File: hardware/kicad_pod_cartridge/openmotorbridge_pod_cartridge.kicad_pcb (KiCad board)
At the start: 2 copper layers, 35 x 25 mm, 28 parts, among them J1 POD_BASE_DOCKING_SOCKET_6P, J2 INTERCOM_HEADSET_6P, Q1 AO3400A, Q2 AO3400A, Q3 AO3400A, Q4 AO3400A, U1 CH32V003F4P6

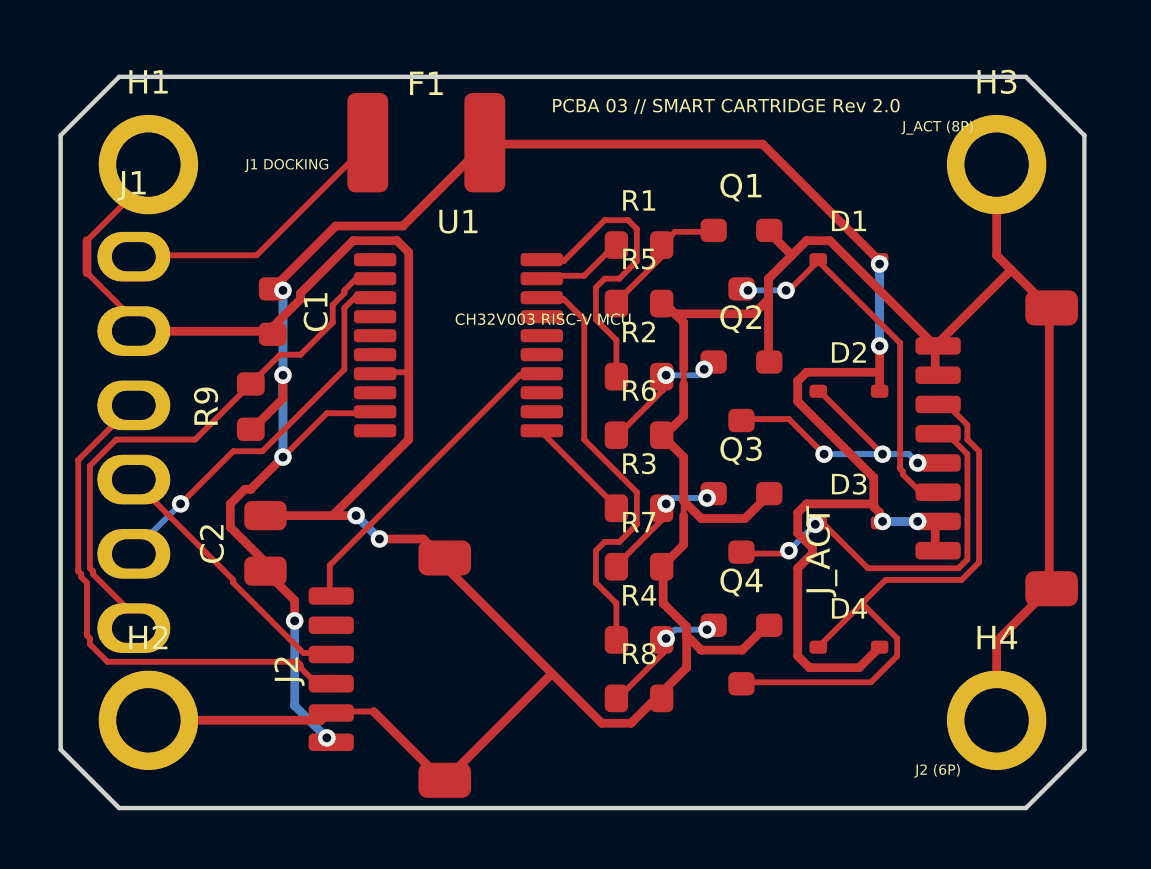
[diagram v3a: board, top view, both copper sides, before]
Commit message: hardware(pcb): synchronize 5-PCBA lineup with v9.6 All-UWB architecture
- PCBA 01 (Central Box): replace obsolete 26-pin IDC header with 12-pin Deutsch DTM-12 header (exact 12-pin net mapping), add 38.4MHz UWB crystal on B.Cu, update silkscreen and schematic
- PCBA 05 (Front Node): place Qorvo DW3110 + U.FL + crystal on B.Cu; place u-blox SAM-M10Q GNSS + Knowles MEMS mic on F.Cu
- PCBA 03 (Pod Cartridge): replace obsolete 6-pin dock socket with PAD1/PAD2 DC spring contact pads; place DW3110 + U.FL on B.Cu
- PCBA 08 (Radar Sub-MCU): update J1 to 2-pin 12V automotive power connector; place DW3110 + U.FL on B.Cu
- PCBA 07 (Smart Keyfob): replace solder pads with 2-pin JST-ACH SMD header (J_QI) for solderless Qi coil connection
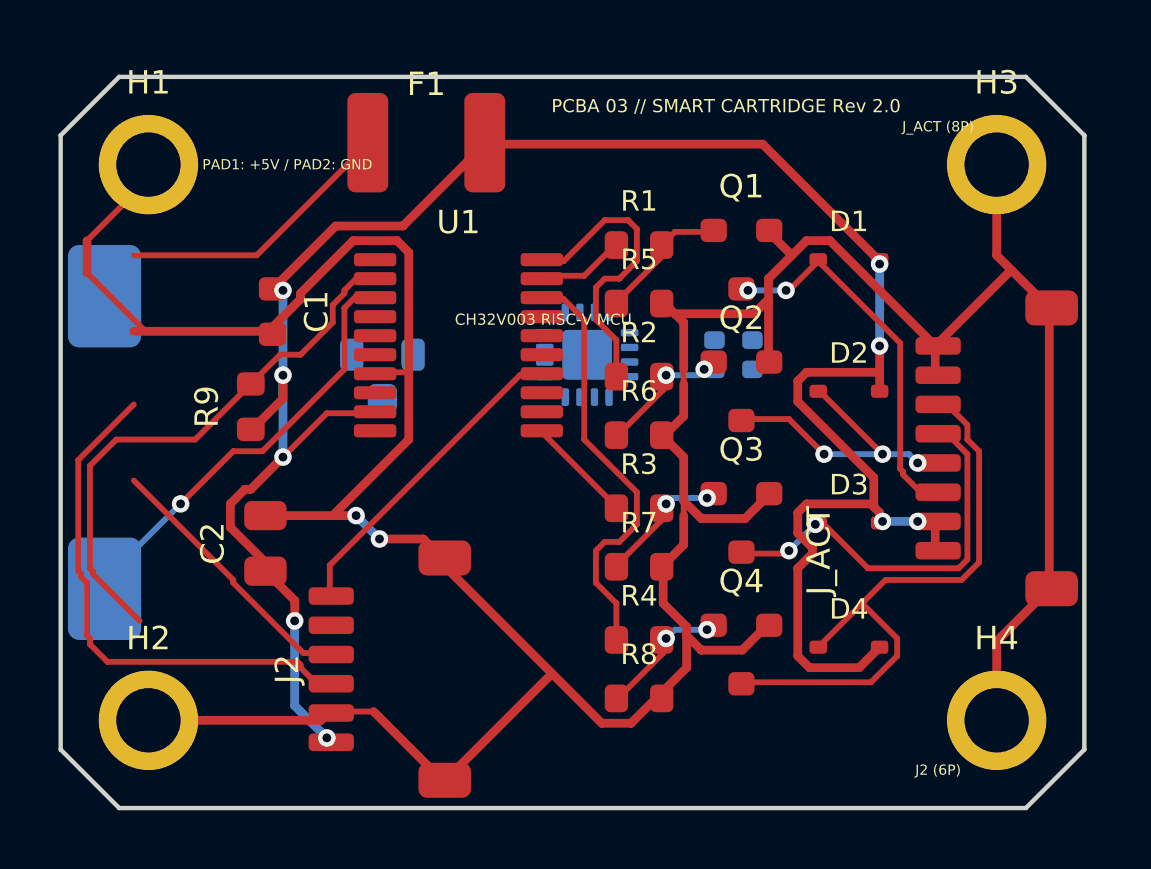
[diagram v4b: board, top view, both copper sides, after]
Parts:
- removed J1: POD_BASE_DOCKING_SOCKET_6P, Connector_PinSocket_2.54mm:PinSocket_1x06_P2.54mm_Horizontal
- added ANT_UWB: Taoglas_FXUWB10, Connector_Coaxial:U.FL_Hirose_U.FL-R-SMT-1_Vertical, B.Cu at (111.0, 77.0)
- added PAD1: +5V_IN, TestPoint:TestPoint_Pad_D3.0mm_OD3.5mm, B.Cu at (101.5, 75.0)
- added PAD2: GND, TestPoint:TestPoint_Pad_D3.0mm_OD3.5mm, B.Cu at (101.5, 85.0)
- added U_UWB: DW3110, Package_DFN_QFN:QFN-16-1EP_3x3mm_P0.5mm_EP1.7x1.7mm_ThermalVias, B.Cu at (118.0, 77.0)
- added Y_UWB: 38.4MHz, Crystal:Crystal_SMD_2016-4Pin_2.0x1.6mm, B.Cu at (123.0, 77.0)
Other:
- board text added: "PAD1: +5V / PAD2: GND"
- board text removed: "J1 DOCKING"
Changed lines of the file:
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@@
 		(embedded_fonts no)
 	)
-	(footprint "Connector_PinSocket_2.54mm:PinSocket_1x06_P2.54mm_Horizontal"
-		(layer "F.Cu")
-		(at 102.5 73.65)
-		(property "Reference" "J1"
+		(footprint "TestPoint:TestPoint_Pad_D3.0mm_OD3.5mm"
+		(layer "B.Cu")
+		(at 101.5 75.0 0)
+		(descr "Mill-Max DC Spring Contact Pad 1 (+5V Power In)")
+		(property "Reference" "PAD1"
 			(at 0 -2.5 0)
-			(layer "F.SilkS")
+			(layer "B.SilkS")
 			(effects
 				(font
@@
 					(thickness 0.12)
 				)
+				(justify mirror)
 			)
 		)
-		(property "Value" "POD_BASE_DOCKING_SOCKET_6P"
-			(at 0 15 0)
-			(layer "F.Fab")
+		(property "Value" "+5V_IN"
+			(at 0 2.5 0)
+			(layer "B.Fab")
 			(effects
 				(font
@@
 					(thickness 0.12)
 				)
+				(justify mirror)
 			)
 		)
-		(property "Datasheet" ""
-			(at 0 0 0)
-			(layer "F.Fab")
-			(hide yes)
+		(pad "1" smd roundrect (at 0 0) (size 2.5 3.5) (layers "B.Cu" "B.Mask") (roundrect_rratio 0.15) (net "VCC_5V"))
+	)
+	(footprint "TestPoint:TestPoint_Pad_D3.0mm_OD3.5mm"
+		(layer "B.Cu")
+		(at 101.5 85.0 0)
+		(descr "Mill-Max DC Spring Contact Pad 2 (GND Return)")
+		(property "Reference" "PAD2"
+			(at 0 -2.5 0)
+			(layer "B.SilkS")
 			(effects
 				(font
-					(size 1.27 1.27)
+					(size 0.8 0.8)
+					(thickness 0.12)
 				)
+				(justify mirror)
 			)
 		)
-		(property "Description" "6-Pin Horizontal Precision Receptacle (Rear Edge Docking to PCBA 02 Pod-Base)"
-			(at 0 0 0)
-			(layer "F.Fab")
-			(hide yes)
+		(property "Value" "GND"
+			(at 0 2.5 0)
+			(layer "B.Fab")
 			(effects
 				(font
-					(size 1.27 1.27)
+					(size 0.8 0.8)
+					(thickness 0.12)
 				)
+				(justify mirror)
 			)
 		)
-		(duplicate_pad_numbers_are_jumpers no)
-		(pad "1" thru_hole oval
-			(at 0 0)
-			(size 2.5 1.7)
-			(drill oval 1.5 1)
-			(layers "*.Cu" "*.Mask")
-			(remove_unused_layers no)
-			(net "POD_VCC")
-		)
-		(pad "2" thru_hole oval
-			(at 0 2.54)
-			(size 2.5 1.7)
-			(drill oval 1.5 1)
-			(layers "*.Cu" "*.Mask")
-			(remove_unused_layers no)
-			(net "GND")
-		)
-		(pad "3" thru_hole oval
-			(at 0 5.08)
-			(size 2.5 1.7)
-			(drill oval 1.5 1)
-			(layers "*.Cu" "*.Mask")
-			(remove_unused_layers no)
-			(net "POD_NF_P")
-		)
-		(pad "4" thru_hole oval
-			(at 0 7.62)
-			(size 2.5 1.7)
-			(drill oval 1.5 1)
-			(layers "*.Cu" "*.Mask")
-			(remove_unused_layers no)
-			(net "POD_NF_N")
-		)
-		(pad "5" thru_hole oval
-			(at 0 10.16)
-			(size 2.5 1.7)
-			(drill oval 1.5 1)
-			(layers "*.Cu" "*.Mask")
-			(remove_unused_layers no)
-			(net "POD_TRIGGER_PPS")
-		)
-		(pad "6" thru_hole oval
-			(at 0 12.7)
-			(size 2.5 1.7)
-			(drill oval 1.5 1)
-			(layers "*.Cu" "*.Mask")
-			(remove_unused_layers no)
-			(net "POD_1WIRE")
-		)
-		(embedded_fonts no)
-		(model "${KICAD10_3DMODEL_DIR}/Connector_PinSocket_2.54mm.3dshapes/PinSocket_1x06_P2.54mm_Horizontal.step"
-			(offset
-				(xyz 0 0 0)
-			)
-			(scale
-				(xyz 1 1 1)
-			)
-			(rotate
-				(xyz 0 0 0)
-			)
-		)
+		(pad "1" smd roundrect (at 0 0) (size 2.5 3.5) (layers "B.Cu" "B.Mask") (roundrect_rratio 0.15) (net "GND"))
 	)
 	(footprint "Diode_SMD:D_SOD-323"
@@
 		(layer "Edge.Cuts")
 	)
-	(gr_text "J1 DOCKING"
+	(gr_text "PAD1: +5V / PAD2: GND"
 		(at 107.75 70.5 0)
 		(layer "F.SilkS")
@@
 	)
 	(embedded_fonts no)
+	(footprint "Package_DFN_QFN:QFN-16-1EP_3x3mm_P0.5mm_EP1.7x1.7mm_ThermalVias"
+		(layer "B.Cu")
+		(at 118 77 180)
+		(descr "Qorvo DW3110 Ultra-Wideband Transceiver")
+		(property "Reference" "U_UWB"
+			(at 0 -2.5 0)
+			(layer "B.SilkS")
+			(effects
+				(font
+					(size 0.8 0.8)
+					(thickness 0.12)
+				)
+				(justify mirror)
+			)
+		)
+		(property "Value" "DW3110"
+			(at 0 2.5 0)
+			(layer "B.Fab")
+			(effects
+				(font
+					(size 0.8 0.8)
+					(thickness 0.12)
+				)
+				(justify mirror)
+			)
+		)
+		(pad "1" smd roundrect (at -1.45 0.75 180) (size 0.6 0.25) (layers "B.Cu" "B.Mask" "B.Paste") (roundrect_rratio 0.25))
+		(pad "2" smd roundrect (at -1.45 0.25 180) (size 0.6 0.25) (layers "B.Cu" "B.Mask" "B.Paste") (roundrect_rratio 0.25))
+		(pad "3" smd roundrect (at -1.45 -0.25 180) (size 0.6 0.25) (layers "B.Cu" "B.Mask" "B.Paste") (roundrect_rratio 0.25))
+		(pad "4" smd roundrect (at -1.45 -0.75 180) (size 0.6 0.25) (layers "B.Cu" "B.Mask" "B.Paste") (roundrect_rratio 0.25))
+		(pad "5" smd roundrect (at -0.75 -1.45 180) (size 0.25 0.6) (layers "B.Cu" "B.Mask" "B.Paste") (roundrect_rratio 0.25))
+		(pad "6" smd roundrect (at -0.25 -1.45 180) (size 0.25 0.6) (layers "B.Cu" "B.Mask" "B.Paste") (roundrect_rratio 0.25))
+		(pad "7" smd roundrect (at 0.25 -1.45 180) (size 0.25 0.6) (layers "B.Cu" "B.Mask" "B.Paste") (roundrect_rratio 0.25))
+		(pad "8" smd roundrect (at 0.75 -1.45 180) (size 0.25 0.6) (layers "B.Cu" "B.Mask" "B.Paste") (roundrect_rratio 0.25))
+		(pad "9" smd roundrect (at 1.45 -0.75 180) (size 0.6 0.25) (layers "B.Cu" "B.Mask" "B.Paste") (roundrect_rratio 0.25))
+		(pad "10" smd roundrect (at 1.45 -0.25 180) (size 0.6 0.25) (layers "B.Cu" "B.Mask" "B.Paste") (roundrect_rratio 0.25))
+		(pad "11" smd roundrect (at 1.45 0.25 180) (size 0.6 0.25) (layers "B.Cu" "B.Mask" "B.Paste") (roundrect_rratio 0.25))
+		(pad "12" smd roundrect (at 1.45 0.75 180) (size 0.6 0.25) (layers "B.Cu" "B.Mask" "B.Paste") (roundrect_rratio 0.25))
+		(pad "13" smd roundrect (at 0.75 1.45 180) (size 0.25 0.6) (layers "B.Cu" "B.Mask" "B.Paste") (roundrect_rratio 0.25))
+		(pad "14" smd roundrect (at 0.25 1.45 180) (size 0.25 0.6) (layers "B.Cu" "B.Mask" "B.Paste") (roundrect_rratio 0.25))
+		(pad "15" smd roundrect (at -0.25 1.45 180) (size 0.25 0.6) (layers "B.Cu" "B.Mask" "B.Paste") (roundrect_rratio 0.25))
+		(pad "16" smd roundrect (at -0.75 1.45 180) (size 0.25 0.6) (layers "B.Cu" "B.Mask" "B.Paste") (roundrect_rratio 0.25))
+		(pad "17" smd roundrect (at 0 0 180) (size 1.7 1.7) (layers "B.Cu" "B.Mask" "B.Paste") (roundrect_rratio 0.1) (net "GND"))
+	)
+	(footprint "Connector_Coaxial:U.FL_Hirose_U.FL-R-SMT-1_Vertical"
+		(layer "B.Cu")
+		(at 111 77 180)
+		(descr "Hirose U.FL Coaxial Connector (Taoglas FXUWB10 Floor Antenna)")
+		(property "Reference" "ANT_UWB"
+			(at 0 -2.5 0)
+			(layer "B.SilkS")
+			(effects
+				(font
+					(size 0.8 0.8)
+					(thickness 0.12)
+				)
+				(justify mirror)
+			)
+		)
+		(property "Value" "Taoglas_FXUWB10"
+			(at 0 2.5 0)
+			(layer "B.Fab")
+			(effects
+				(font
+					(size 0.8 0.8)
+					(thickness 0.12)
+				)
+				(justify mirror)
+			)
+		)
+		(pad "1" smd roundrect (at 0 -1.5 180) (size 1.0 1.0) (layers "B.Cu" "B.Mask" "B.Paste") (roundrect_rratio 0.25))
+		(pad "2" smd roundrect (at -1.05 0 180) (size 0.8 1.1) (layers "B.Cu" "B.Mask" "B.Paste") (roundrect_rratio 0.25) (net "GND"))
+		(pad "2" smd roundrect (at 1.05 0 180) (size 0.8 1.1) (layers "B.Cu" "B.Mask" "B.Paste") (roundrect_rratio 0.25) (net "GND"))
+	)
+	(footprint "Crystal:Crystal_SMD_2016-4Pin_2.0x1.6mm"
+		(layer "B.Cu")
+		(at 123 77 180)
+		(descr "SMD Crystal 38.4MHz 2.0x1.6mm 4-Pin")
+		(property "Reference" "Y_UWB"
+			(at 0 -1.5 0)
+			(layer "B.SilkS")
+			(effects
+				(font
+					(size 0.7 0.7)
+					(thickness 0.12)
+				)
+				(justify mirror)
+			)
+		)
+		(property "Value" "38.4MHz"
+			(at 0 1.5 0)
+			(layer "B.Fab")
+			(effects
+				(font
+					(size 0.7 0.7)
+					(thickness 0.12)
+				)
+				(justify mirror)
+			)
+		)
+		(pad "1" smd roundrect (at -0.65 0.5 180) (size 0.7 0.6) (layers "B.Cu" "B.Mask" "B.Paste") (roundrect_rratio 0.25))
+		(pad "2" smd roundrect (at 0.65 0.5 180) (size 0.7 0.6) (layers "B.Cu" "B.Mask" "B.Paste") (roundrect_rratio 0.25) (net "GND"))
+		(pad "3" smd roundrect (at 0.65 -0.5 180) (size 0.7 0.6) (layers "B.Cu" "B.Mask" "B.Paste") (roundrect_rratio 0.25))
+		(pad "4" smd roundrect (at -0.65 -0.5 180) (size 0.7 0.6) (layers "B.Cu" "B.Mask" "B.Paste") (roundrect_rratio 0.25) (net "GND"))
+	)
 )

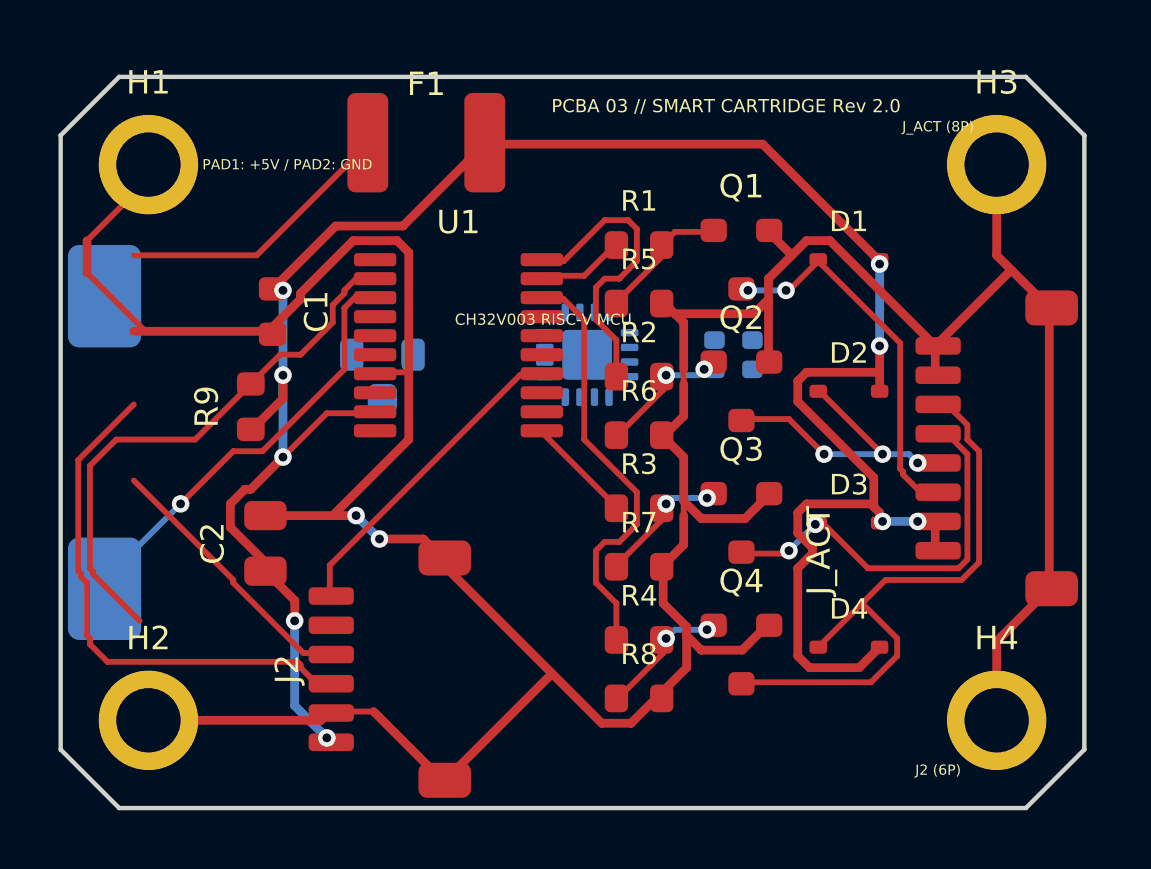
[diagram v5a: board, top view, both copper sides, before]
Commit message: feat(audio): genuinely integrate Qualcomm QCC3084 BT 5.4 Audio SoC for dual-helmet aptX HD link
- Hardware (PCBA 01): Placed U9 (Qualcomm QCC3084 module with onboard ceramic antenna) at (175, 106) on F.Cu; wired I2S bus, UART, and reset/enable controls in mcu_codec_can.kicad_sch.
- Firmware: Upgraded bluetooth_audio_manager to full QCC3084 driver supporting Dual-A2DP aptX HD/Adaptive, LE Audio Auracast, independent AVRCP volume, and modal HFP 1.8 telephony interceptor.
- Docs: Updated 02_intercom_matrix_profiles, 07_pcba_hardware_pinouts, and 09_firmware_architecture with technical specs and pinout tables for the dedicated Qualcomm audio link.
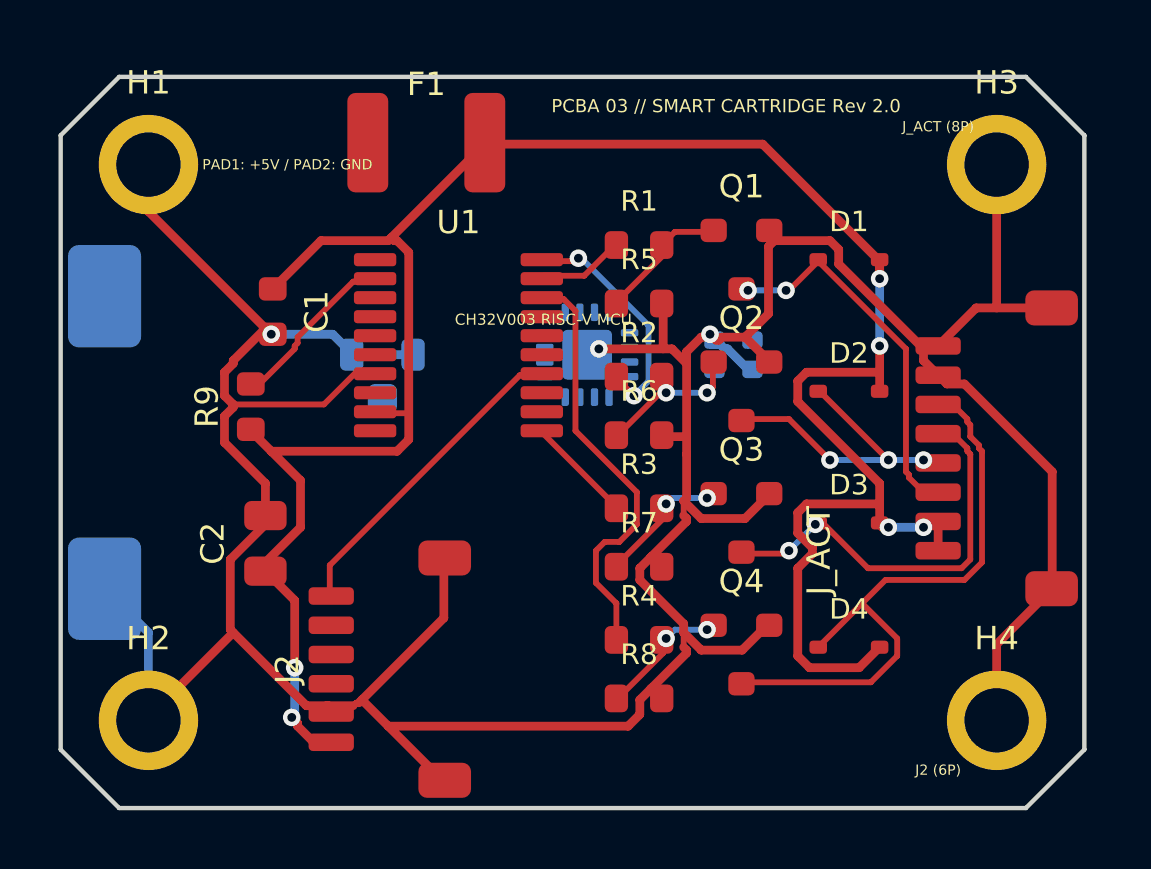
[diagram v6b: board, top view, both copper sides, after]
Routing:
- net POD_NF_P: track 18.0 -> 0.00 mm
- net POD_TRIGGER_PPS: track 13.2 -> 0.00 mm, vias 1 -> 0
- net POD_1WIRE: track 18.9 -> 6.02 mm
- net POD_VCC: track 9.62 -> 0.00 mm
- net GND: track 126.2 -> 135.6 mm, vias 2 -> 3
- net POD_NF_N: track 9.27 -> 0.00 mm
- net VCC_5V_PROT: track 76.3 -> 79.6 mm, vias 9 -> 6
- net ACT2_GATE: track 10.4 -> 8.39 mm, vias 0 -> 2
- net Q2_GATE: track 4.65 -> 5.42 mm

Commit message: feat(hardware): integrate Everest Semi ES8388 24-bit audio codec (U3) on PCBA 03 cartridge
- Schematic: Added Audio:ES8388 symbol and instance U3 connected to J2 (intercom audio in/out) and I2S/I2C.
- PCB: Placed U3 (QFN-28 4x4mm) at (107.5, 71.0) on F.Cu between H1 and F1 with zero overlaps.
- Renders: Generated updated 3D renders (perspective, top, and doc render) showing the integrated codec.
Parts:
- added U3: ES8388_Codec, Package_DFN_QFN:QFN-28-1EP_4x4mm_P0.4mm_EP2.4x2.4mm, F.Cu at (107.5, 71.0)

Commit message: hardware(cartridge): move ES8388 audio codec to B.Cu bottom layer to eliminate overlaps and isolate from actuator MOSFETs
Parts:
- U3: moved to B.Cu
- moved U3 15.0 mm to (115.0, 84.0), turned to 180 degrees
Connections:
- U3 pad 1: I2S_MCLK -> (no net)
- U3 pad 10: AUDIO_OUT_P -> (no net)
- U3 pad 11: AUDIO_OUT_N -> (no net)
- U3 pad 12: AGND -> (no net)
- U3 pad 13: AUDIO_IN_P -> (no net)
- U3 pad 14: AUDIO_IN_N -> (no net)
- U3 pad 15: AGND -> (no net)
- U3 pad 16: VCC_3V3 -> (no net)
- U3 pad 17: AGND -> (no net)
- U3 pad 2: I2S_BCLK -> (no net)
- U3 pad 28: VCC_3V3 -> (no net)
- U3 pad 29: GND_PWR -> (no net)
- U3 pad 3: I2S_WS -> (no net)
- U3 pad 4: I2S_DIN -> (no net)
- U3 pad 5: I2S_DOUT -> (no net)
- U3 pad 6: I2C_SCL -> (no net)
- U3 pad 7: I2C_SDA -> (no net)
- U3 pad 8: VCC_3V3 -> (no net)
- U3 pad 9: GND_PWR -> (no net)
